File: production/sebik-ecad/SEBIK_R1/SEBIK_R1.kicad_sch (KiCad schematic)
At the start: 87 parts, among them J1 Conn_01x06_Male, J10 Conn_01x02_Male, J11 Conn_01x03_Male, J11 USB_B, J12 Conn_01x02_Male, J13 Conn_01x02_Male, J2 Conn_01x02_Male, J3 Conn_01x02_Male, J4 Conn_01x02_Male, J5 Conn_01x02_Male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

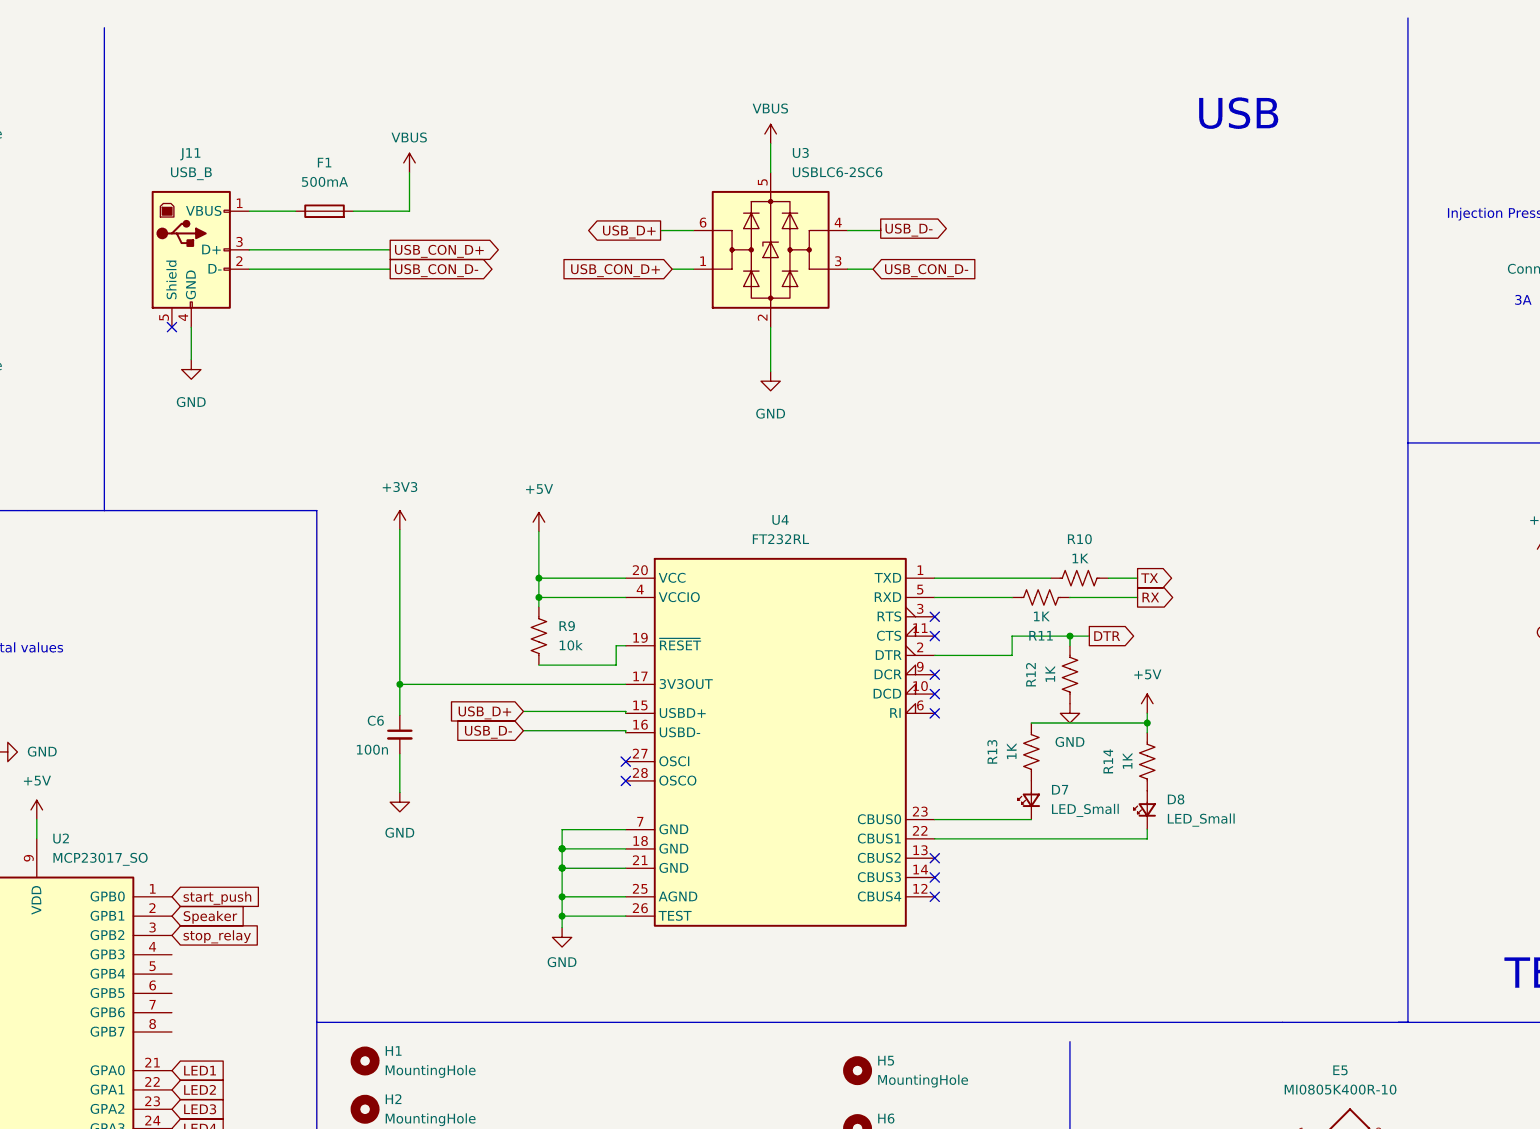
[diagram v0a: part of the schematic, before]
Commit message: changed microUSB to USBC
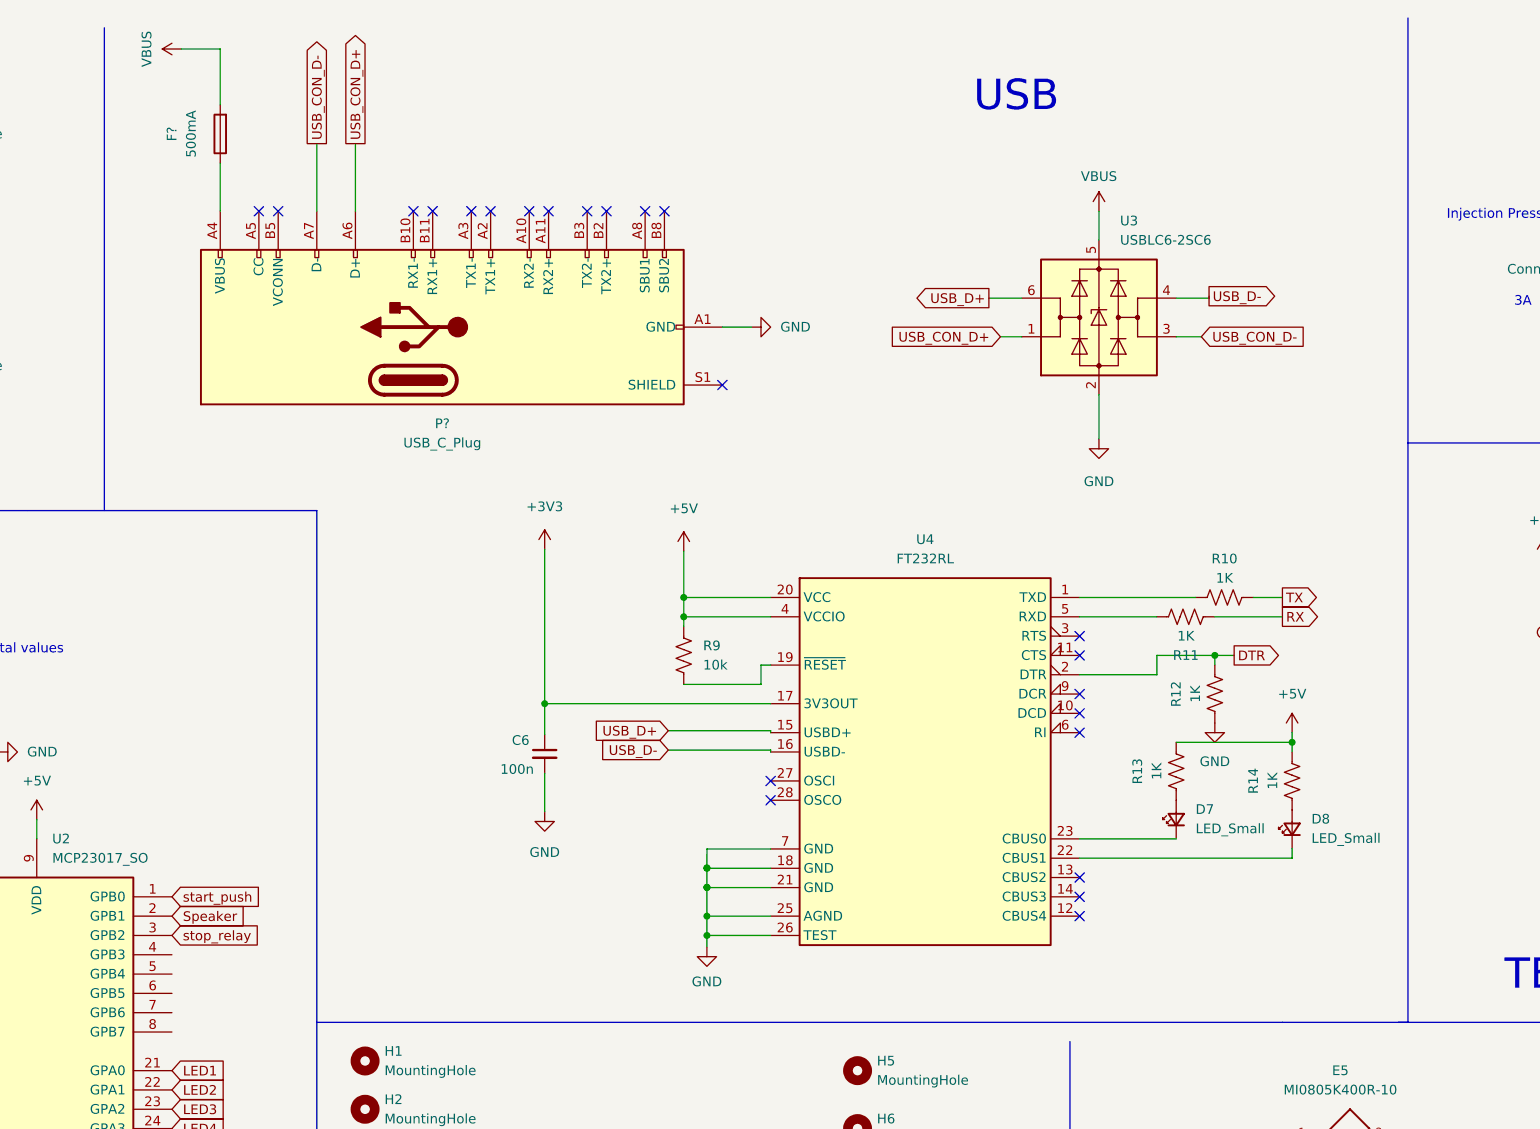
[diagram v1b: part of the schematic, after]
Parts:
- removed F1: 500mA, Fuse:Fuse_1210_3225Metric, symbol Device:Fuse
- removed J11: USB_B, Connector_USB:USB_Micro-B_Amphenol_10104110_Horizontal, symbol Connector:USB_B
- added F?: 500mA, Fuse:Fuse_1210_3225Metric, symbol Device:Fuse
- added P?: USB_C_Plug, symbol Connector:USB_C_Plug
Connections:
- net GND: now also P?.A1 (GND), P?.A12 (GND), P?.B1 (GND), P?.B12 (GND)
- net USB_CON_D+: now also P?.A6 (D+)
- net USB_CON_D-: now also P?.A7 (D-)
- net VBUS: now also F?.2
- new net: F?.1, P?.A4 (VBUS), P?.A9 (VBUS), P?.B4 (VBUS), P?.B9 (VBUS)
- no-connect marks 11 -> 23
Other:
- moved on the sheet: C6, D7, D8, R10, R11, R12, R13, R14, R9, U3, U4
